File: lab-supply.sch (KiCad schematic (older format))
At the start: 47 parts, among them Q1 Q_NPN_BCE, U1 MP8862GQ, U2 INA220, U3 MAX1719EUT

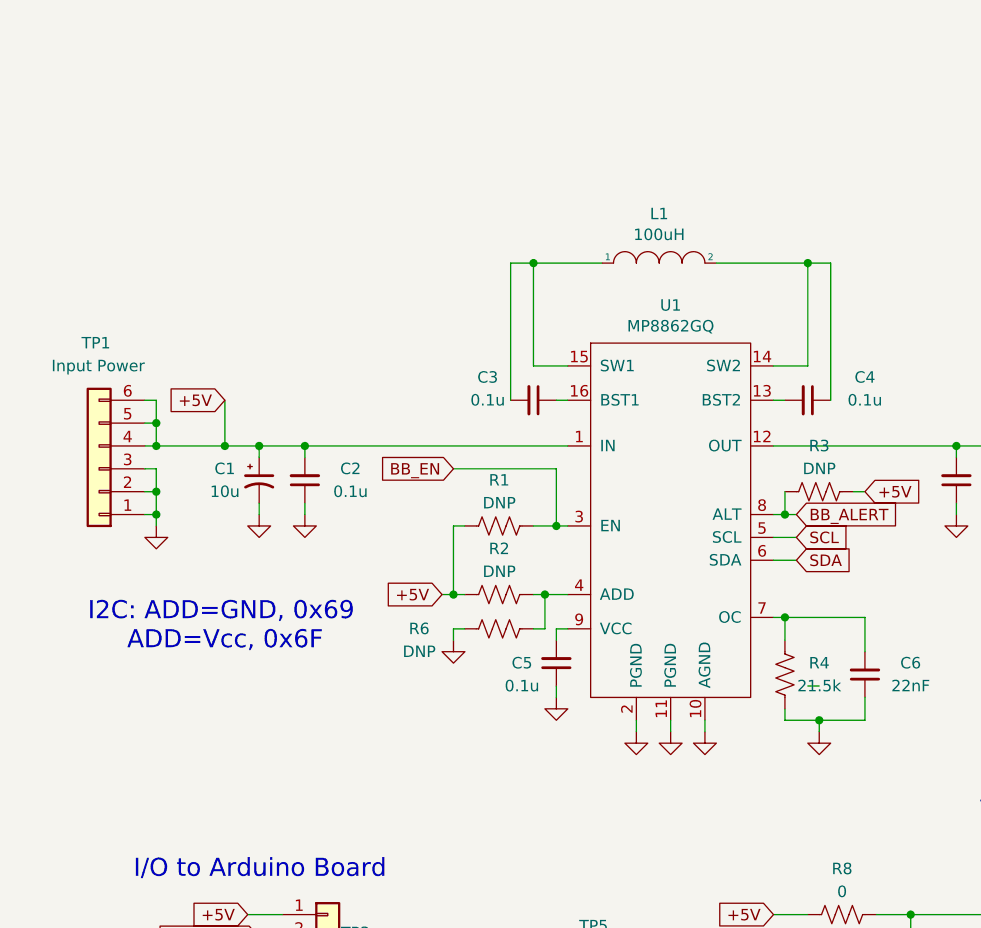
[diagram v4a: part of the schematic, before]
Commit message: Separated Vcc_bb from 5V
Allows for buck/boost to run off of separate Vin from the rest of the circuit. For example +12V
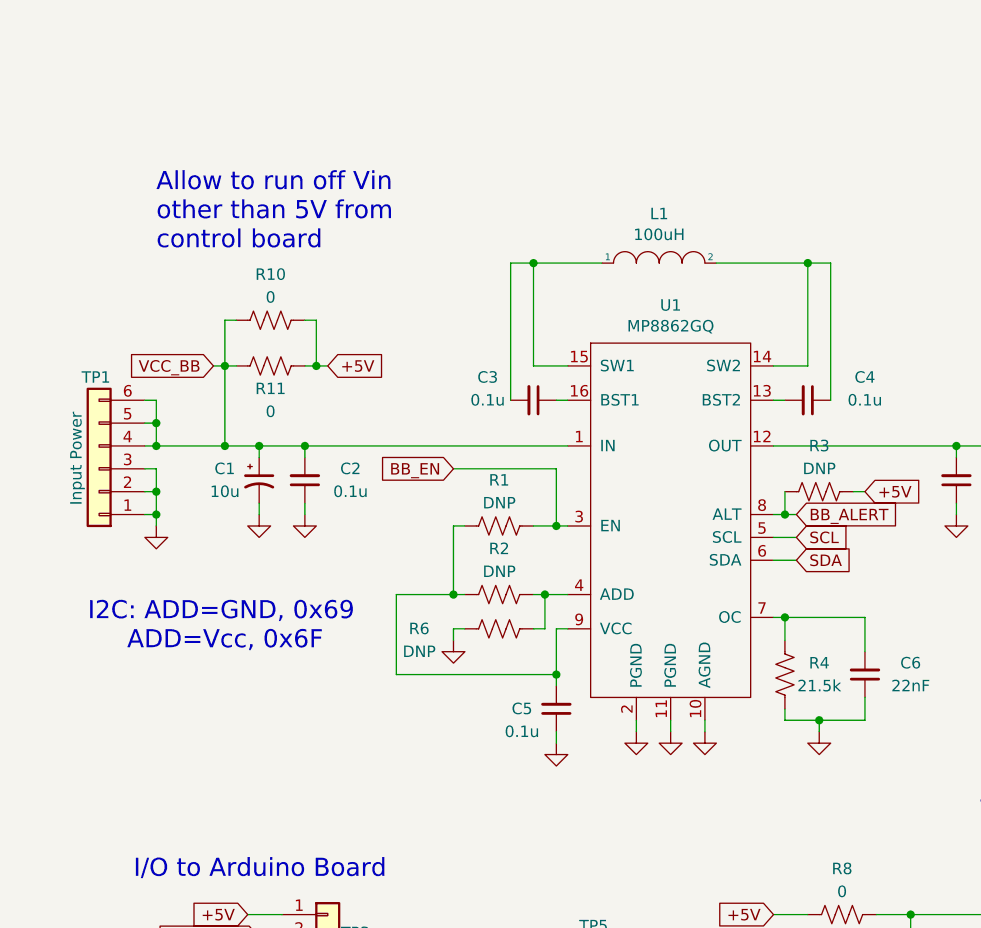
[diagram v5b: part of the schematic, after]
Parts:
- added R10, R11: 0, Rays Footprints:R_0805_HandSoldering, symbol Device:R_US
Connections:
- net +5V: now also R10.1, R11.1; no longer C1.1, C2.2, R1.2, R2.2, TP1.4 (Pin_4), TP1.5 (Pin_5), TP1.6 (Pin_6), U1.1 (IN)
- net at C5.2, U1.9 (VCC): now also R1.2, R2.2
- new net VCC_BB: C1.1, C2.2, R10.2, R11.2, TP1.4 (Pin_4), TP1.5 (Pin_5), TP1.6 (Pin_6), U1.1 (IN)
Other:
- note added: "Allow to run off Vin\nother than 5V from\ncontrol board"
- moved on the sheet: C5
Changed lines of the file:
@@
 Wire Wire Line
 	2650 2750 2650 2800
-Text GLabel 2300 2300 0    50   Input ~ 0
-+5V
+Text GLabel 2250 2150 0    50   Input ~ 0
+VCC_BB
 Connection ~ 2450 2500
 $Comp
 L Device:C_Small C5
 U 1 1 5EF72D37
-P 3750 3450
-F 0 "C5" H 3900 3450 50  0000 C CNN
-F 1 "0.1u" H 3900 3550 50  0000 C CNN
-F 2 "Rays Footprints:C_0603_HandSoldering" H 3750 3450 50  0001 C CNN
-F 3 "~" H 3750 3450 50  0001 C CNN
-	1    3750 3450
+P 3750 3650
+F 0 "C5" H 3900 3650 50  0000 C CNN
+F 1 "0.1u" H 3900 3750 50  0000 C CNN
+F 2 "Rays Footprints:C_0603_HandSoldering" H 3750 3650 50  0001 C CNN
+F 3 "~" H 3750 3650 50  0001 C CNN
+	1    3750 3650
 	-1   0    0    1
 $EndComp
@@
 L power:GND #PWR05
 U 1 1 5EF72D41
-P 3750 3600
-F 0 "#PWR05" H 3750 3350 50  0001 C CNN
-F 1 "GND" H 3755 3427 50  0001 C CNN
-F 2 "" H 3750 3600 50  0001 C CNN
-F 3 "" H 3750 3600 50  0001 C CNN
-	1    3750 3600
-	1    0    0    -1
-$EndComp
-Wire Wire Line
-	3750 3550 3750 3600
+P 3750 3800
+F 0 "#PWR05" H 3750 3550 50  0001 C CNN
+F 1 "GND" H 3755 3627 50  0001 C CNN
+F 2 "" H 3750 3800 50  0001 C CNN
+F 3 "" H 3750 3800 50  0001 C CNN
+	1    3750 3800
+	1    0    0    -1
+$EndComp
+Wire Wire Line
+	3750 3750 3750 3800
 Wire Wire Line
 	3800 3300 3750 3300
-Wire Wire Line
-	3750 3300 3750 3350
 $Comp
 L Device:R_US R2
@@
 Wire Wire Line
 	3800 3150 3700 3150
-Text GLabel 3250 3150 0    50   Input ~ 0
-+5V
-Wire Wire Line
-	3250 3150 3300 3150
 $Comp
 L Device:R_US R1
@@
 	4900 3700 4750 3700
 Wire Wire Line
-	4850 3550 4900 3550
-Wire Wire Line
 	5900 2500 5900 2550
 $Comp
@@
 U 1 1 5F3A352E
 P 1750 2600
-F 0 "TP1" H 1700 2050 50  0000 L CNN
-F 1 "Input Power" H 1550 2150 50  0000 L CNN
+F 0 "TP1" H 1700 2200 50  0000 L CNN
+F 1 "Input Power" V 1850 2350 50  0000 L CNN
 F 2 "Connector_PinHeader_2.54mm:PinHeader_1x06_P2.54mm_Vertical" H 1950 2600 50  0001 C CNN
 F 3 "" H 1950 2600 50  0001 C CNN
@@
 	-1   0    0    1
 $EndComp
-Wire Wire Line
-	2300 2300 2300 2500
 Connection ~ 2300 2500
 Wire Wire Line
@@
 Wire Wire Line
 	8900 2600 8900 2750
+Wire Wire Line
+	3750 3300 3750 3500
+Wire Wire Line
+	3750 3500 3050 3500
+Wire Wire Line
+	3050 3500 3050 3150
+Wire Wire Line
+	3050 3150 3300 3150
+Connection ~ 3750 3500
+Wire Wire Line
+	3750 3500 3750 3550
+$Comp
+L Device:R_US R11
+U 1 1 5EDBEE35
+P 2500 2150
+F 0 "R11" V 2600 2150 50  0000 C CNN
+F 1 "0" V 2700 2150 50  0000 C CNN
+F 2 "Rays Footprints:R_0805_HandSoldering" V 2540 2140 50  0001 C CNN
+F 3 "https://www.digikey.com/product-detail/en/stackpole-electronics-inc/RMCF1210JT12R0/RMCF1210JT12R0CT-ND/7906987" H 2500 2150 50  0001 C CNN
+	1    2500 2150
+	0    1    1    0
+$EndComp
+Wire Wire Line
+	2300 2150 2300 2500
+Wire Wire Line
+	2250 2150 2300 2150
+Wire Wire Line
+	2350 2150 2300 2150
+Connection ~ 2300 2150
+Text GLabel 2750 2150 2    50   Input ~ 0
++5V
+Wire Wire Line
+	2700 2150 2650 2150
+$Comp
+L Device:R_US R10
+U 1 1 5EDE3305
+P 2500 1950
+F 0 "R10" V 2300 1950 50  0000 C CNN
+F 1 "0" V 2400 1950 50  0000 C CNN
+F 2 "Rays Footprints:R_0805_HandSoldering" V 2540 1940 50  0001 C CNN
+F 3 "https://www.digikey.com/product-detail/en/stackpole-electronics-inc/RMCF1210JT12R0/RMCF1210JT12R0CT-ND/7906987" H 2500 1950 50  0001 C CNN
+	1    2500 1950
+	0    1    1    0
+$EndComp
+Wire Wire Line
+	2300 2150 2300 1950
+Wire Wire Line
+	2300 1950 2350 1950
+Wire Wire Line
+	2650 1950 2700 1950
+Wire Wire Line
+	2700 1950 2700 2150
+Wire Wire Line
+	2700 2150 2750 2150
+Connection ~ 2700 2150
+Text Notes 2000 1650 0    79   ~ 0
+Allow to run off Vin\nother than 5V from\ncontrol board
 $EndSCHEMATC
